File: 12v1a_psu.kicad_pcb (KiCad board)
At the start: 4 copper layers, 100 x 160 mm, 23 parts, among them J1 AC_IN, J2 P1, J3 P2, J4 Vout, Q1 TIP32AG, U1 L7812

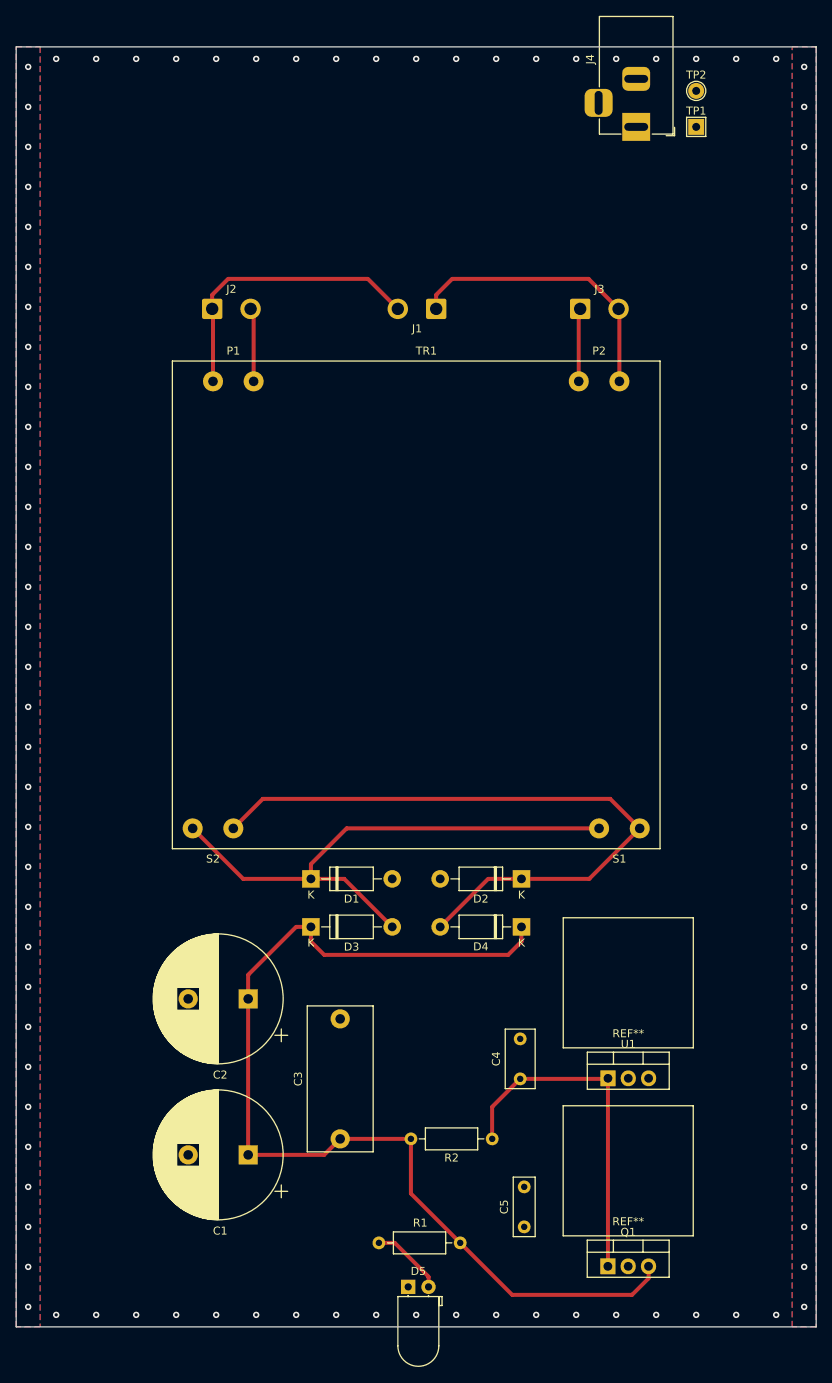
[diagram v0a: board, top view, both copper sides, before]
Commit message: Add switch blockout for assembly check, misc layout change
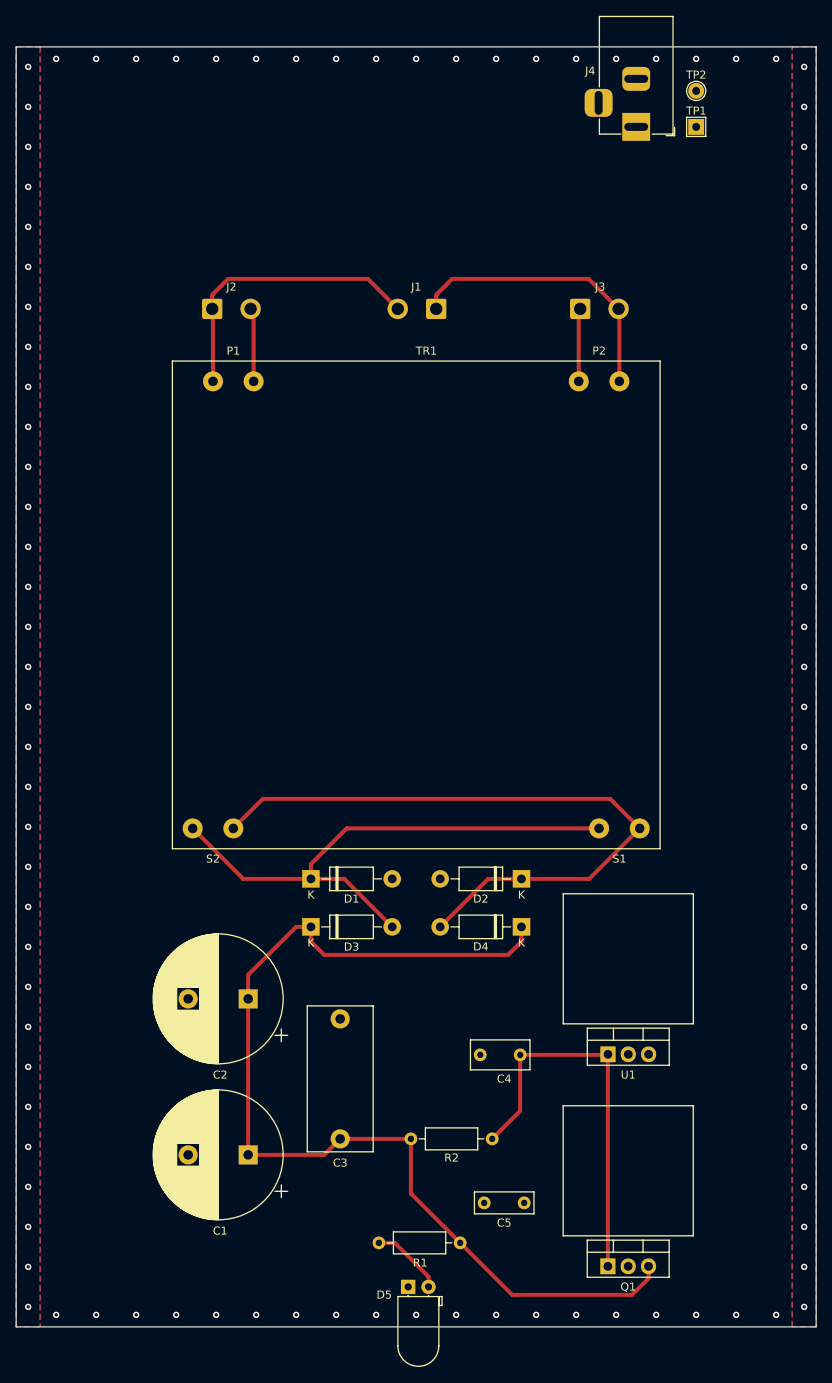
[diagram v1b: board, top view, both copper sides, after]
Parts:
- moved C4 3.00 mm to (103.0, 151.0), turned to 180 degrees
- moved C5 3.00 mm to (103.5, 169.5), turned to 180 degrees
- moved REF** 3.00 mm to (116.5, 147.1)
- moved U1 3.00 mm to (114.0, 150.9)
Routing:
- net Net-(C4-Pad1): track 43.5 -> 49.5 mm

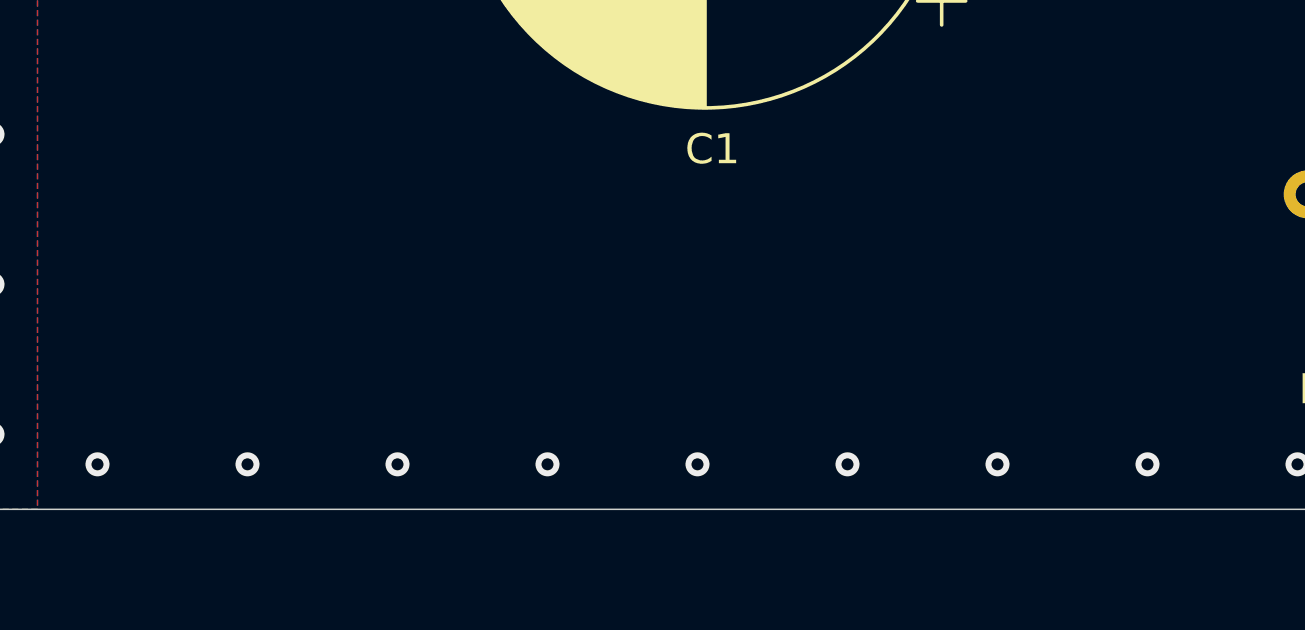
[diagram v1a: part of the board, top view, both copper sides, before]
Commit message: Add cat silkscreen, update sheet info
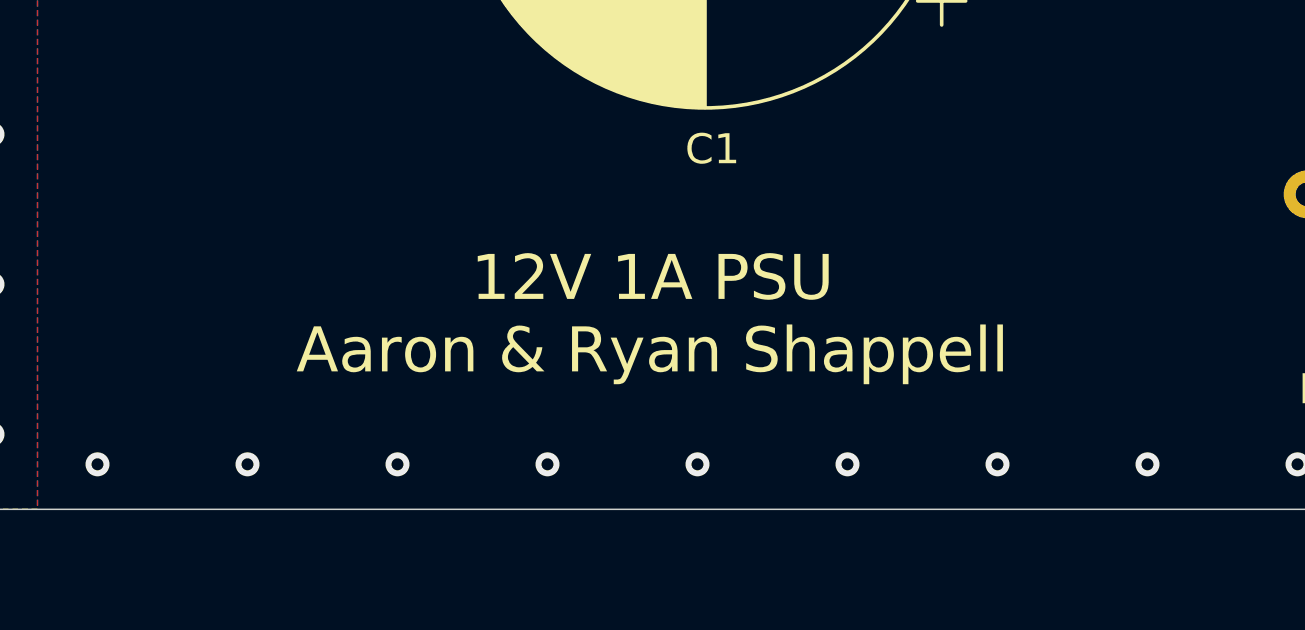
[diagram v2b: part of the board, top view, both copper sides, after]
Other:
- board text added: "12V 1A PSU Aaron & Ryan Shappell"
